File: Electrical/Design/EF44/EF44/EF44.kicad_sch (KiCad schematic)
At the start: 0 parts

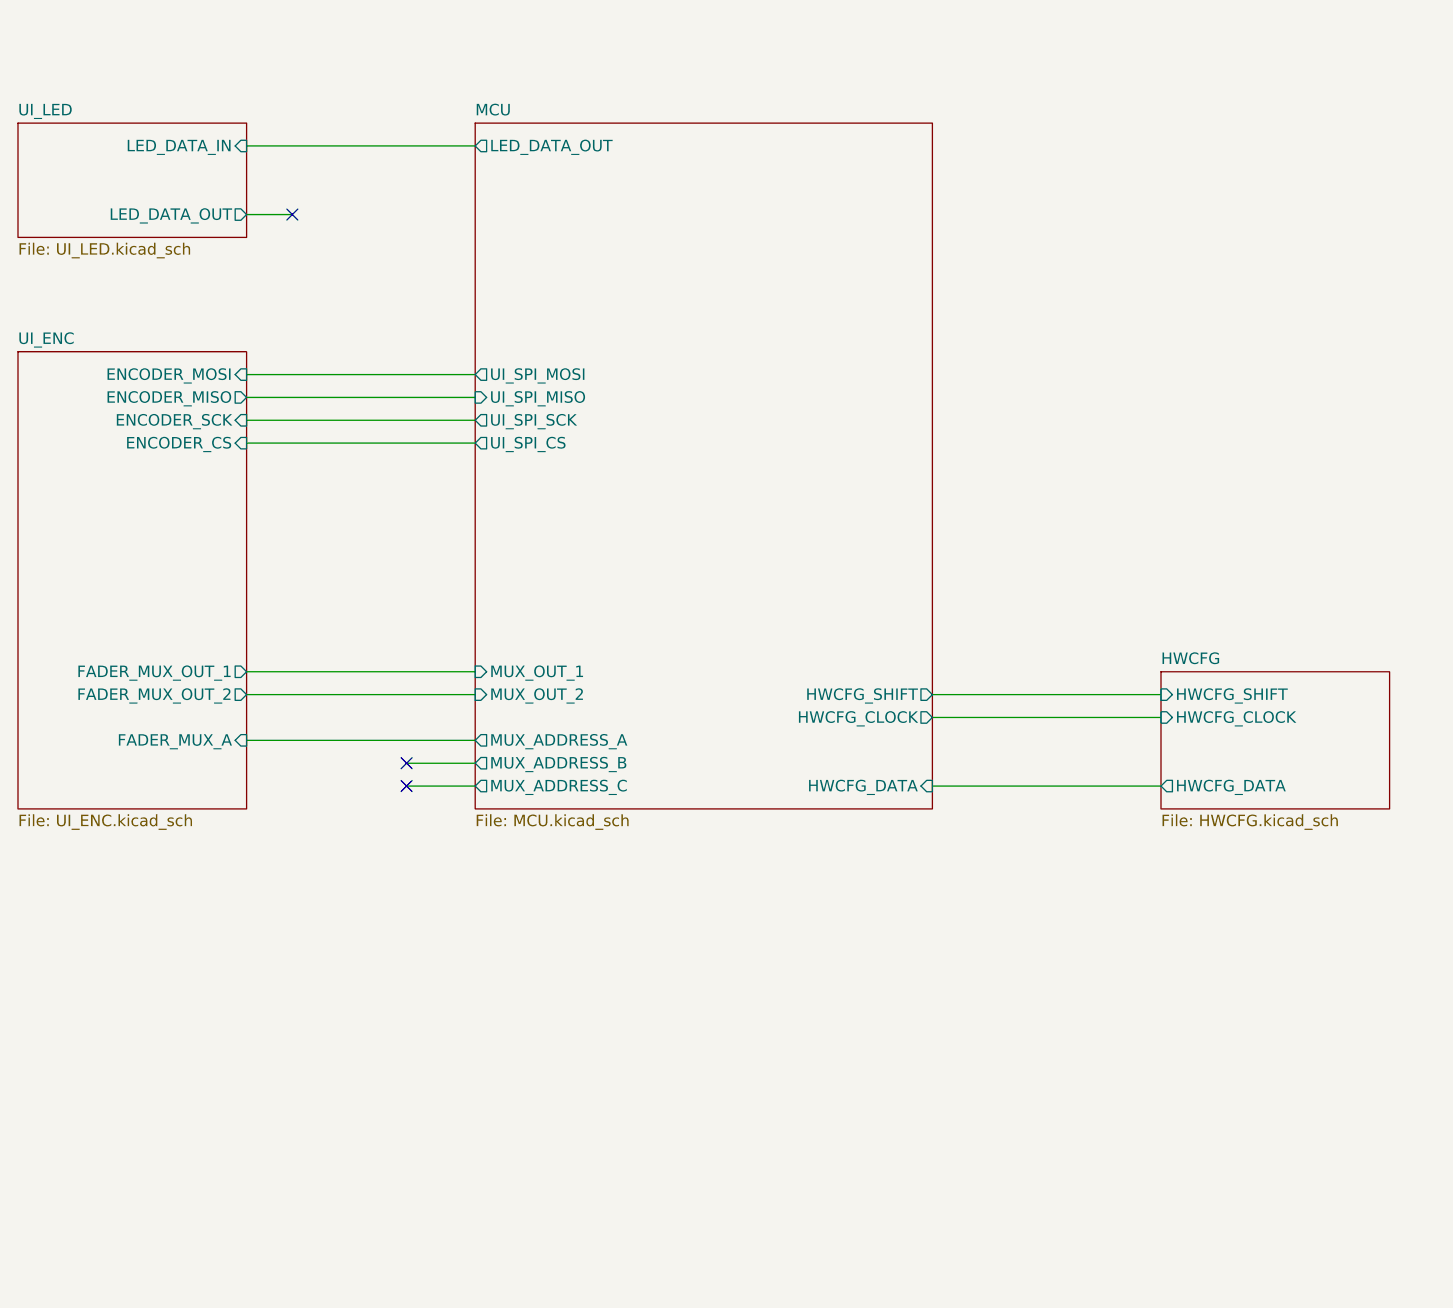
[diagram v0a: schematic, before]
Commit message: SUKU EF44 created from EN16 Base
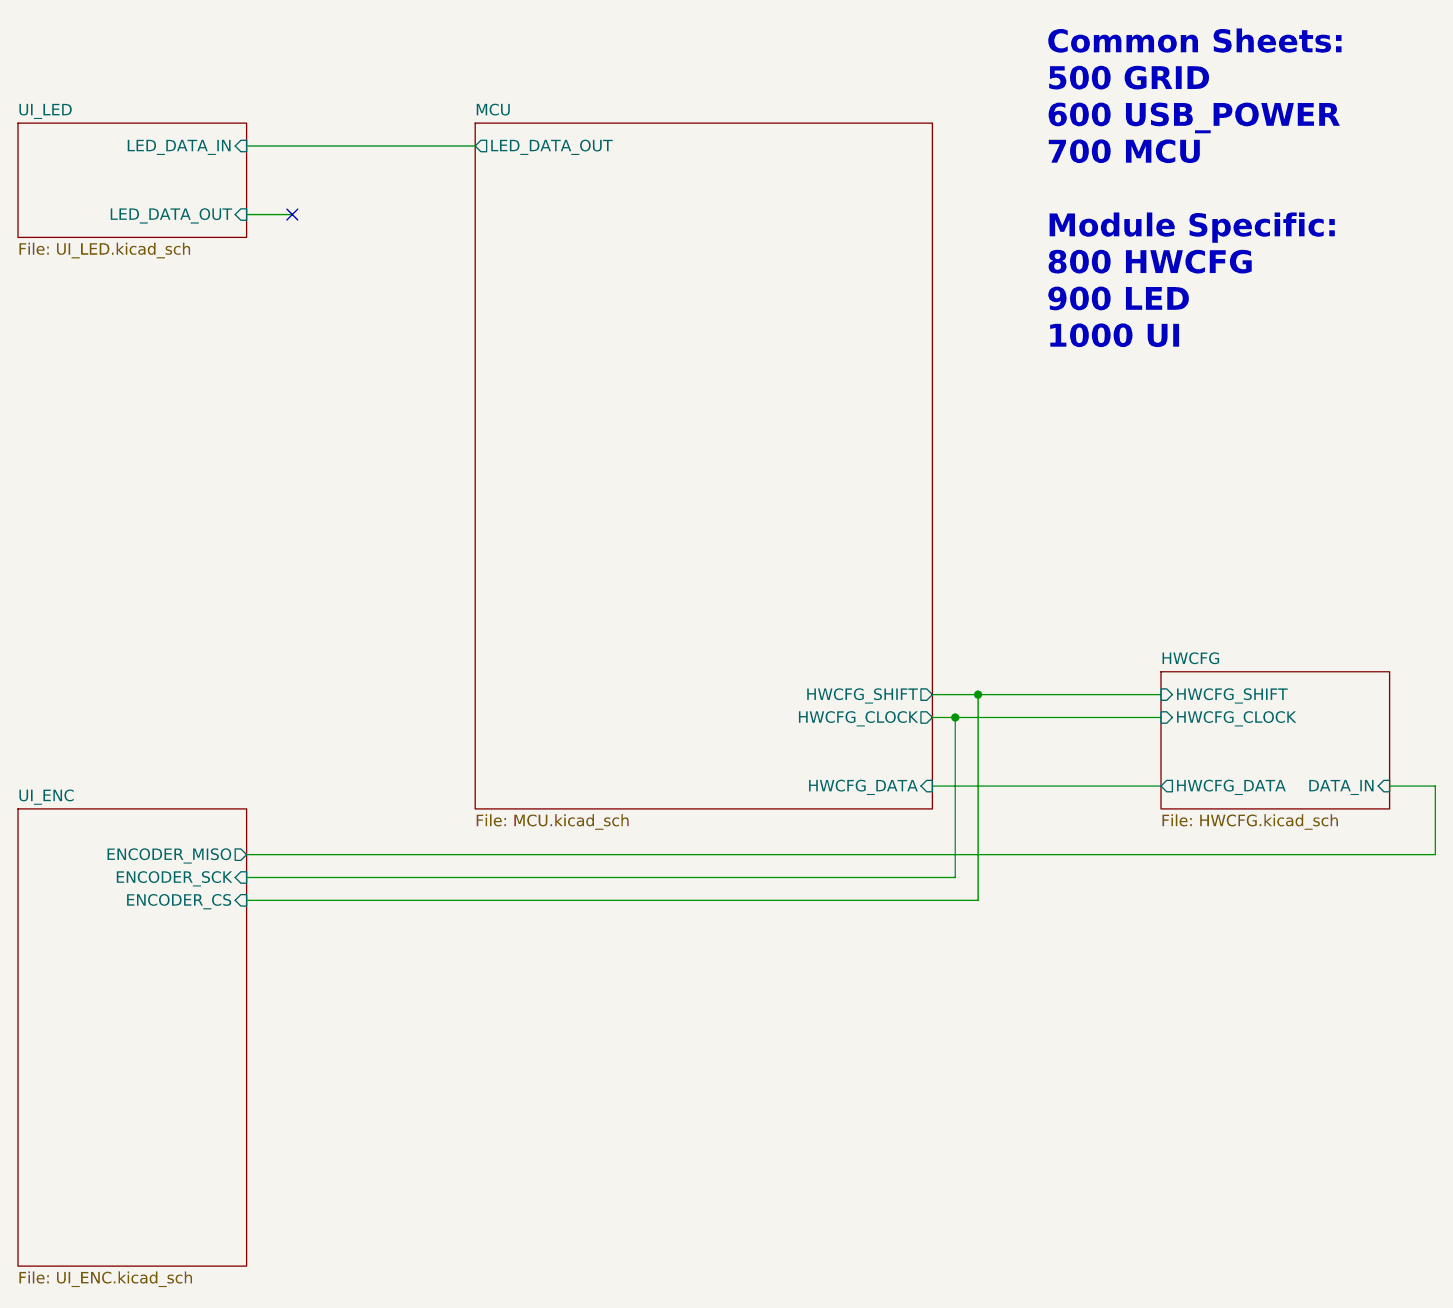
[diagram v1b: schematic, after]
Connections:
- no-connect marks 3 -> 1
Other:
- sheet HWCFG ports: added DATA_IN; removed none
- sheet MCU ports: added none; removed MUX_ADDRESS_A, MUX_ADDRESS_B, MUX_ADDRESS_C, MUX_OUT_1, MUX_OUT_2, UI_SPI_CS, UI_SPI_MISO, UI_SPI_MOSI, UI_SPI_SCK
- sheet UI_ENC ports: added none; removed ENCODER_MOSI, FADER_MUX_A, FADER_MUX_OUT_1, FADER_MUX_OUT_2
- note added: "Common Sheets: 500 GRID 600 USB_POWER 700 MCU Module Specific: 800 HWCFG 900 LED 1000 UI"

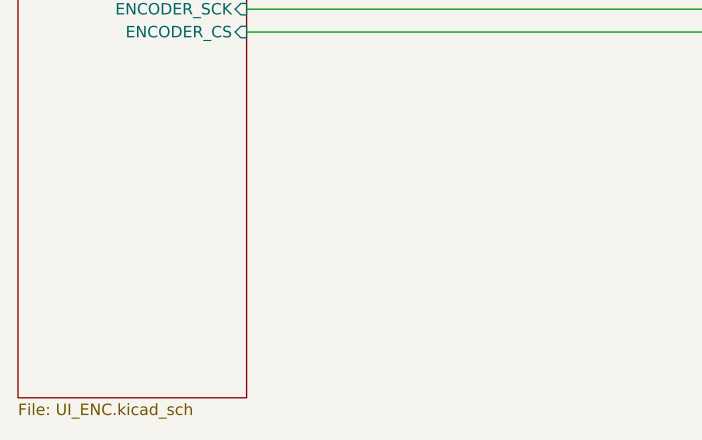
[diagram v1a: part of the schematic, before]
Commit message: SUKU EF44 component positions done
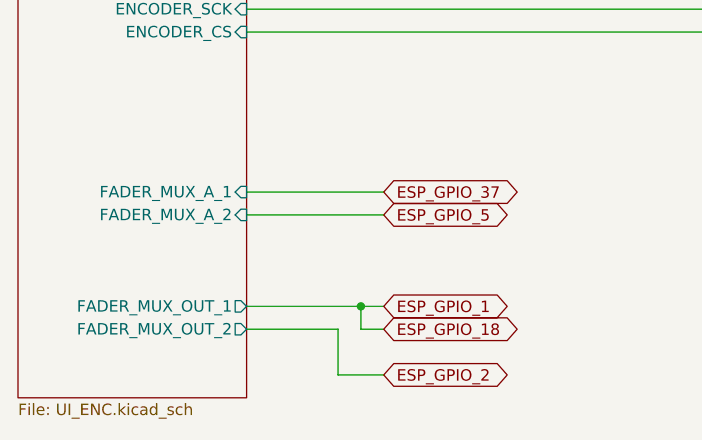
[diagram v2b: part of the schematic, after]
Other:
- sheet UI_ENC ports: added FADER_MUX_A_1, FADER_MUX_A_2, FADER_MUX_OUT_1, FADER_MUX_OUT_2; removed none
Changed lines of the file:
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@@
   (junction (at 281.94 167.64) (diameter 0) (color 0 0 0 0)
   )
+  (junction (at 215.9 218.44) (diameter 0) (color 0 0 0 0)
+  )
   (junction (at 284.48 165.1) (diameter 0) (color 0 0 0 0)
   )
   (no_connect (at 208.28 111.76))
+  (wire (pts (xy 203.2 205.74) (xy 218.44 205.74))
+    (stroke (width 0) (type default))
+  )
   (wire (pts (xy 203.2 182.88) (xy 335.28 182.88))
     (stroke (width 0) (type default))
   )
+  (wire (pts (xy 215.9 220.98) (xy 215.9 218.44))
+    (stroke (width 0) (type default))
+  )
   (wire (pts (xy 279.4 165.1) (xy 284.48 165.1))
     (stroke (width 0) (type default))
@@
     (stroke (width 0) (type default))
   )
+  (wire (pts (xy 215.9 218.44) (xy 218.44 218.44))
+    (stroke (width 0) (type default))
+  )
   (wire (pts (xy 284.48 165.1) (xy 304.8 165.1))
     (stroke (width 0) (type default))
@@
     (stroke (width 0) (type default))
   )
+  (wire (pts (xy 213.36 220.98) (xy 203.2 220.98))
+    (stroke (width 0) (type default))
+  )
+  (wire (pts (xy 218.44 226.06) (xy 213.36 226.06))
+    (stroke (width 0) (type default))
+  )
   (wire (pts (xy 279.4 175.26) (xy 304.8 175.26))
     (stroke (width 0) (type default))
   )
+  (wire (pts (xy 213.36 226.06) (xy 213.36 220.98))
+    (stroke (width 0) (type default))
+  )
   (wire (pts (xy 203.2 187.96) (xy 284.48 187.96))
     (stroke (width 0) (type default))
@@
   )
   (wire (pts (xy 279.4 167.64) (xy 281.94 167.64))
+    (stroke (width 0) (type default))
+  )
+  (wire (pts (xy 218.44 220.98) (xy 215.9 220.98))
+    (stroke (width 0) (type default))
+  )
+  (wire (pts (xy 203.2 218.44) (xy 215.9 218.44))
+    (stroke (width 0) (type default))
+  )
+  (wire (pts (xy 203.2 208.28) (xy 218.44 208.28))
     (stroke (width 0) (type default))
   )
@@
     (effects (font (size 2.54 2.54) (thickness 0.508) bold) (justify left bottom))
   )
+  (global_label "ESP_GPIO_5" (shape bidirectional) (at 218.44 208.28 0) (fields_autoplaced)
+    (effects (font (size 1.27 1.27)) (justify left))
+    (property "Intersheetrefs" "${INTERSHEET_REFS}" (at 232.0128 208.2006 0)
+      (effects (font (size 1.27 1.27)) (justify left) hide)
+    )
+  )
+  (global_label "ESP_GPIO_18" (shape bidirectional) (at 218.44 220.98 0) (fields_autoplaced)
+    (effects (font (size 1.27 1.27)) (justify left))
+    (property "Intersheetrefs" "${INTERSHEET_REFS}" (at 233.2223 220.9006 0)
+      (effects (font (size 1.27 1.27)) (justify left) hide)
+    )
+  )
+  (global_label "ESP_GPIO_1" (shape bidirectional) (at 218.44 218.44 0) (fields_autoplaced)
+    (effects (font (size 1.27 1.27)) (justify left))
+    (property "Intersheetrefs" "${INTERSHEET_REFS}" (at 232.0128 218.3606 0)
+      (effects (font (size 1.27 1.27)) (justify left) hide)
+    )
+  )
+  (global_label "ESP_GPIO_2" (shape bidirectional) (at 218.44 226.06 0) (fields_autoplaced)
+    (effects (font (size 1.27 1.27)) (justify left))
+    (property "Intersheetrefs" "${INTERSHEET_REFS}" (at 232.0128 225.9806 0)
+      (effects (font (size 1.27 1.27)) (justify left) hide)
+    )
+  )
+  (global_label "ESP_GPIO_37" (shape bidirectional) (at 218.44 205.74 0) (fields_autoplaced)
+    (effects (font (size 1.27 1.27)) (justify left))
+    (property "Intersheetrefs" "${INTERSHEET_REFS}" (at 233.2223 205.6606 0)
+      (effects (font (size 1.27 1.27)) (justify left) hide)
+    )
+  )
   (sheet (at 177.8 101.6) (size 25.4 12.7) (fields_autoplaced)
     (stroke (width 0) (type solid))
@@
     )
     (instances
-      (project "EN16"
+      (project "EF44"
         (path "/e5217a0c-7f55-4c30-adda-7f8d95709d1b" (page "4"))
       )
@@
     )
     (instances
-      (project "EN16"
+      (project "EF44"
         (path "/e5217a0c-7f55-4c30-adda-7f8d95709d1b" (page "7"))
       )
@@
     )
     (instances
-      (project "EN16"
+      (project "EF44"
         (path "/e5217a0c-7f55-4c30-adda-7f8d95709d1b" (page "10"))
       )
@@
     )
     (pin "ENCODER_CS" input (at 203.2 187.96 0)
+      (effects (font (size 1.27 1.27)) (justify right))
+    )
+    (pin "FADER_MUX_OUT_1" output (at 203.2 218.44 0)
+      (effects (font (size 1.27 1.27)) (justify right))
+    )
+    (pin "FADER_MUX_OUT_2" output (at 203.2 220.98 0)
+      (effects (font (size 1.27 1.27)) (justify right))
+    )
+    (pin "FADER_MUX_A_1" input (at 203.2 205.74 0)
+      (effects (font (size 1.27 1.27)) (justify right))
+    )
+    (pin "FADER_MUX_A_2" input (at 203.2 208.28 0)
       (effects (font (size 1.27 1.27)) (justify right))
     )
@@
         (path "/1fbb0219-551e-409b-a61b-76e8cebdfb9d" (page "3"))
       )
-      (project "EN16"
+      (project "EF44"
         (path "/e5217a0c-7f55-4c30-adda-7f8d95709d1b" (page "13"))
       )
